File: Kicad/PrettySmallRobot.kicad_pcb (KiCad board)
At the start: 4 copper layers, 26 x 29 mm, 51 parts, among them J1 TYPE-C-31-M-12, J10 Conn_01x02, J8 Conn_01x02, J9 Conn_01x02, U1 DRV8837, U2 DRV8837, U3 MCP73831-2-OT, U4 ESP32-S2, U6 AP2112K-3.3, Y1 12pF/40MHz

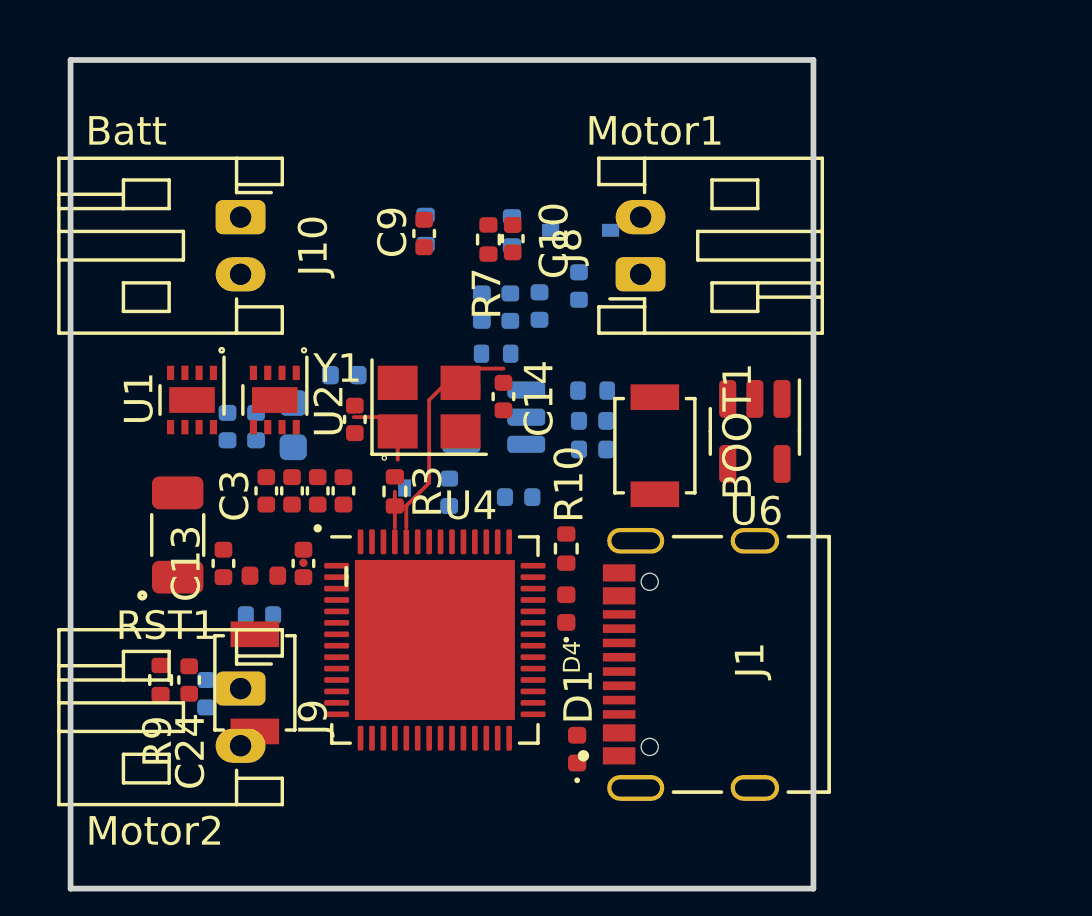
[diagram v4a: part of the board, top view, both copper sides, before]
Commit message: added keeput area for clip sections
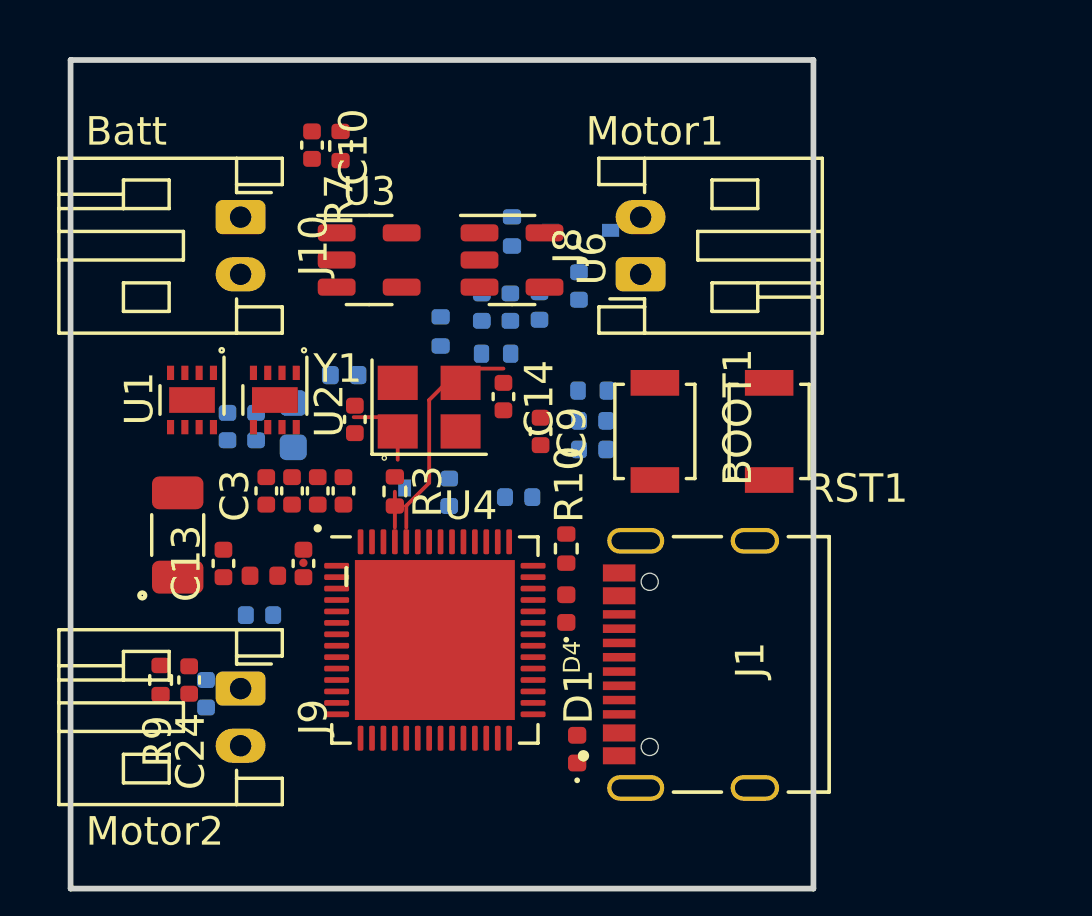
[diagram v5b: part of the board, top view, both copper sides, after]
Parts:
- U3: moved to F.Cu
- moved RST1 20.0 mm to (195.5, 110.5), turned to -90 degrees
- moved U6 10.4 mm to (186.5, 104.5), turned to 0 degrees
- moved C9 8.04 mm to (187.5, 110.5), turned to 90 degrees
- moved C10 7.75 mm to (179.5, 100.5)
- moved U3 7.02 mm to (181.5, 104.5), turned to 0 degrees
- moved R7 6.12 mm to (180.5, 100.5)
- moved R2 3.59 mm to (184.0, 107.0)
- moved BOOT1 0.50 mm to (191.5, 110.5)
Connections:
- J10 pad 1: unconnected-(J10-Pad1) -> +BATT
- J10 pad 2: unconnected-(J10-Pad2) -> GND
- J8 pad 1: unconnected-(J8-Pad1) -> /MOTORA_OUT1
- J8 pad 2: unconnected-(J8-Pad2) -> /MOTORA_OUT2
- J9 pad 1: unconnected-(J9-Pad1) -> /MOTORB_OUT1
- J9 pad 2: unconnected-(J9-Pad2) -> /MOTORB_OUT2

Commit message: floorplanning 50% done
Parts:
- C2, C24, C3, C6, C7, C9, R9, U1, U2: moved to B.Cu
- C22, C23: moved to F.Cu
- moved C24 22.5 mm to (196.0, 110.5)
- moved R9 22.5 mm to (195.0, 110.5)
- moved C23 20.7 mm to (186.5, 102.0), turned to 180 degrees
- moved C3 19.5 mm to (194.0, 101.5), turned to 180 degrees
- moved U2 16.7 mm to (194.0, 104.0)
- moved C22 16.4 mm to (184.5, 102.0), turned to 0 degrees
- moved C2 14.7 mm to (194.0, 106.5), turned to 180 degrees
- moved C18 13.7 mm to (183.5, 119.5)
- moved C19 13.7 mm to (184.5, 119.5)
- moved C20 13.7 mm to (182.5, 119.5)
- moved R2 12.4 mm to (192.5, 116.0)
- moved C7 12.1 mm to (173.5, 123.0), turned to 180 degrees
- moved U1 11.2 mm to (173.6, 120.5)
- moved C5 11.0 mm to (186.0, 116.0)
- moved D3 10.5 mm to (182.0, 101.0)
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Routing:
- net Net-(C14-Pad2): track 7.85 -> 0.00 mm
- net Net-(C15-Pad1): track 3.03 -> 0.00 mm
- net Net-(R3-Pad2): track 1.25 -> 0.00 mm

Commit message: routing started
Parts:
- R5: moved to F.Cu
- moved D1 21.1 mm to (184.5, 101.0), turned to 180 degrees
- moved C16 9.79 mm to (186.5, 119.5), turned to 90 degrees
- moved C11 9.20 mm to (185.5, 119.5), turned to 90 degrees
- moved R5 8.55 mm to (186.5, 101.0), turned to 0 degrees
- moved C19 4.59 mm to (181.5, 116.0), turned to -90 degrees
- moved C20 3.67 mm to (183.5, 116.0), turned to -90 degrees
- moved C18 3.66 mm to (182.5, 116.0), turned to -90 degrees
- moved L1 2.00 mm to (182.0, 117.5), turned to 180 degrees
- moved C1 1.92 mm to (183.7, 118.5)
- moved C4 1.50 mm to (185.0, 117.5), turned to 90 degrees
- moved C5 1.50 mm to (186.0, 117.5), turned to 90 degrees
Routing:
- net /D+: track 0.00 -> 11.8 mm
- net /D-: track 0.00 -> 11.2 mm
- net Net-(C14-Pad2): track 0.00 -> 7.85 mm
- net /VDD3P3: track 0.00 -> 4.47 mm, vias 0 -> 1
- net /VDDA: track 0.00 -> 4.21 mm, vias 0 -> 1
- net +3V3: track 0.00 -> 3.73 mm
- net /VDD_SPI: track 0.00 -> 3.27 mm, vias 0 -> 1
- net Net-(C15-Pad1): track 0.00 -> 3.16 mm
- net Net-(AE1-Pad1): track 0.00 -> 2.55 mm
- net Net-(C17-Pad1): track 0.00 -> 2.08 mm
- net Net-(R3-Pad2): track 0.00 -> 1.25 mm
- net GND: vias 0 -> 34

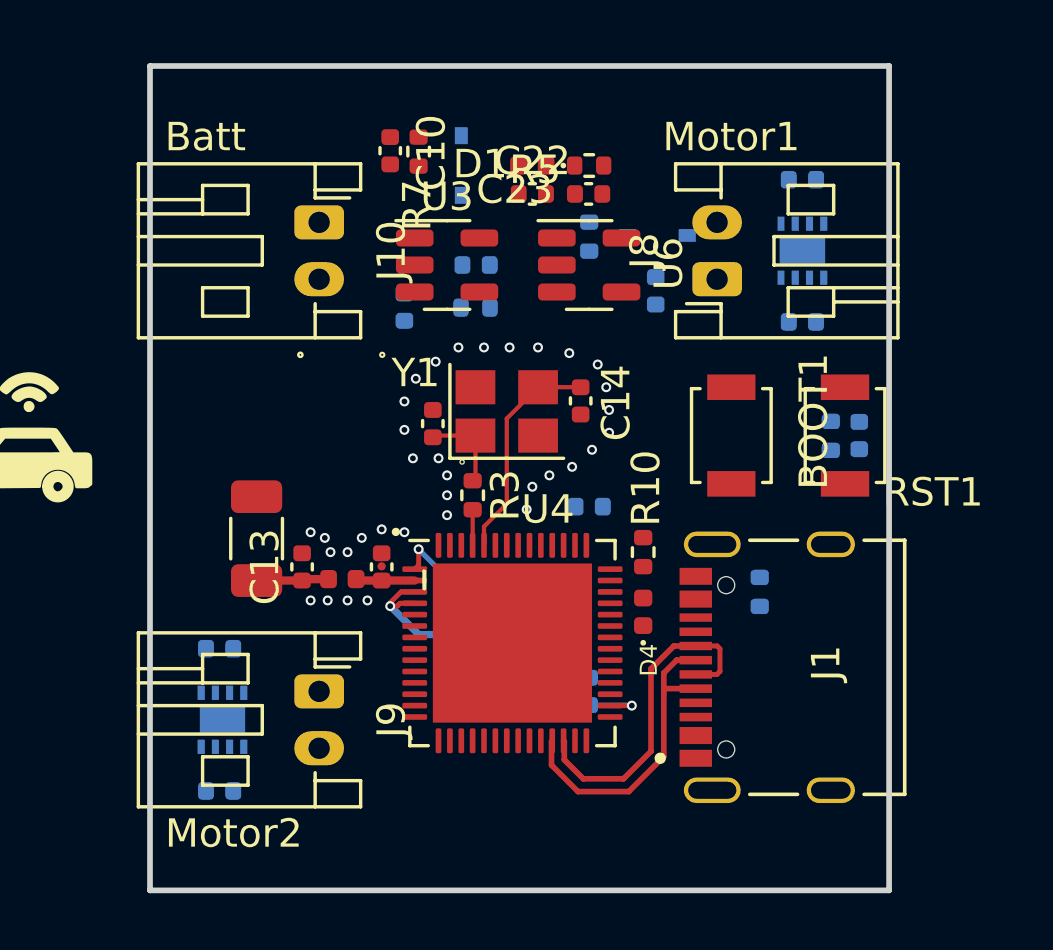
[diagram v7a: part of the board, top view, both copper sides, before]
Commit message: swapped motor a and b connectors
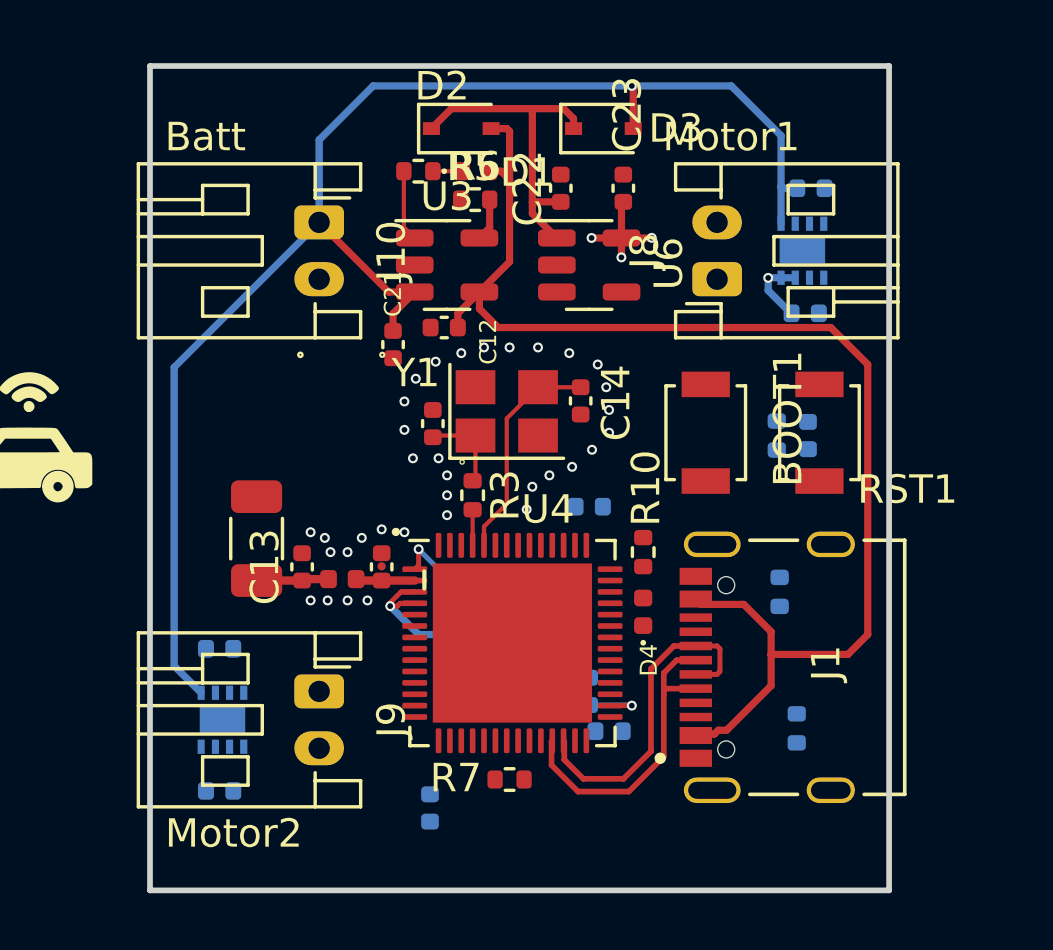
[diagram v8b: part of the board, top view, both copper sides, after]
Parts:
- C10: moved to B.Cu
- C12, C21, D2, D3, R6: moved to F.Cu
- moved R7 22.3 mm to (183.7, 122.6), turned to 180 degrees
- moved C10 21.8 mm to (187.2, 120.9), turned to 0 degrees
- moved C8 19.8 mm to (180.9, 123.6)
- moved R1 18.8 mm to (193.8, 120.8)
- moved D2 7.86 mm to (182.0, 99.7), turned to 0 degrees
- moved R5 6.01 mm to (180.5, 101.2), turned to 180 degrees
- moved D3 5.17 mm to (187.0, 99.7), turned to 0 degrees
- moved C2 4.71 mm to (194.3, 101.8), turned to 0 degrees
- moved C3 4.70 mm to (194.1, 106.2), turned to 0 degrees
- moved R6 3.80 mm to (182.5, 102.2), turned to 0 degrees
- moved C12 2.47 mm to (181.4, 106.7)
- moved D1 2.02 mm to (182.5, 101.2), turned to 0 degrees
- moved R9 1.90 mm to (193.1, 110.5)
- moved C24 1.80 mm to (194.2, 110.5)
- moved C21 1.38 mm to (179.6, 107.3)
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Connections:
- J8 pad 1: /MOTORA_OUT1 -> /MOTORB_OUT1
- J8 pad 2: /MOTORA_OUT2 -> /MOTORB_OUT2
- J9 pad 1: /MOTORB_OUT1 -> /MOTORA_OUT1
- J9 pad 2: /MOTORB_OUT2 -> /MOTORA_OUT2
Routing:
- net +BATT: track 0.00 -> 51.0 mm, vias 0 -> 1
- net /VBUS: track 0.00 -> 46.4 mm
- net Net-(C22-Pad1): track 0.00 -> 11.7 mm
- net +3V3: track 3.73 -> 10.4 mm, vias 0 -> 4
- net Net-(R5-Pad2): track 0.00 -> 2.51 mm
- net Net-(R6-Pad2): track 0.00 -> 1.50 mm
- net Net-(D1-Pad1): track 0.00 -> 1.00 mm
